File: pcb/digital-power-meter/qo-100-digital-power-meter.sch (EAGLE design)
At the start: 32 parts, among them U1 F2915NBGK, U2 ADP7142AUJZ-3.3

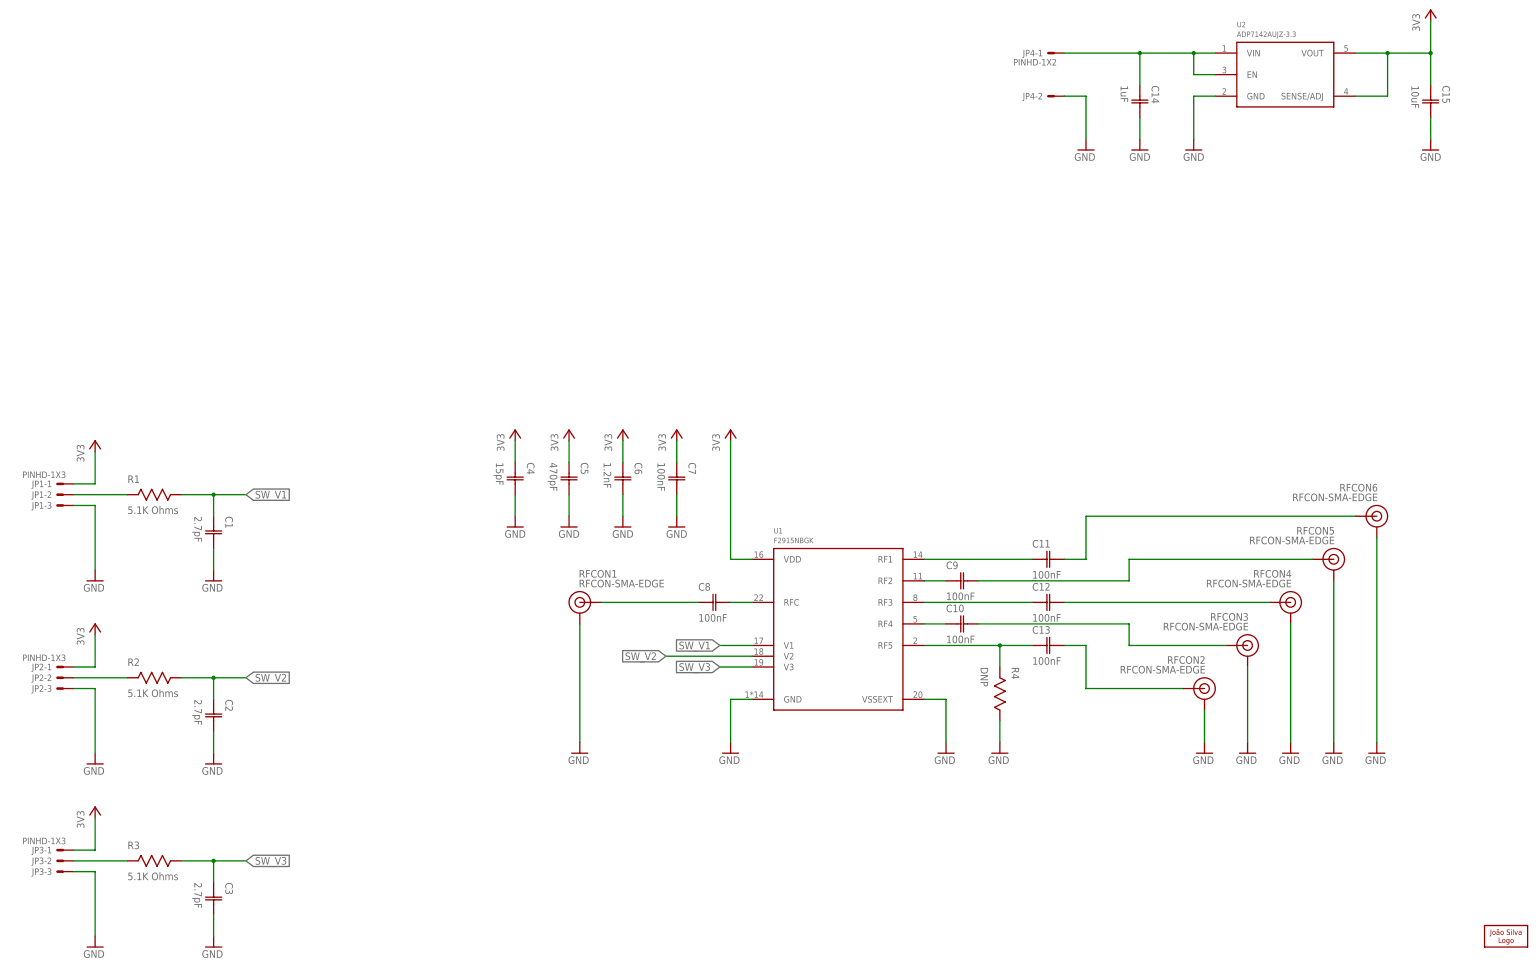
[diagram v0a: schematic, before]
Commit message: Finished RF switch Added Digital RF power detector Added Orange Pi control hat
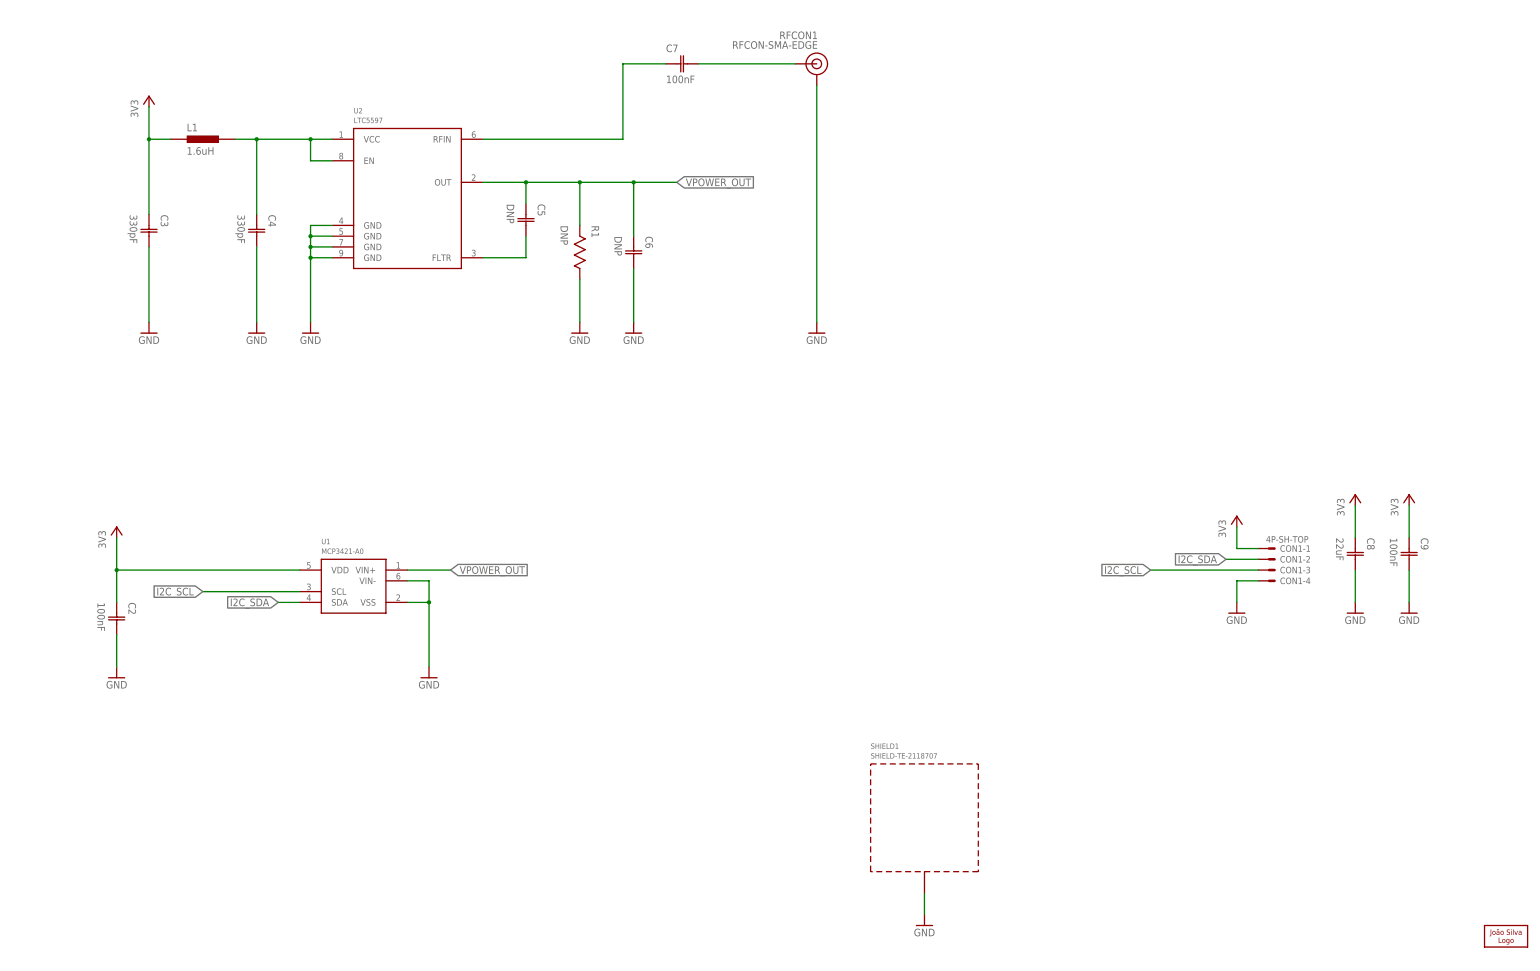
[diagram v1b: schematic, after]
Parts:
- removed C1: 2.7pF, Capacitor:CAPACITOR-0603
- removed C10, C11, C12, C13: 100nF, Capacitor:CAPACITOR-0603
- removed C14: 1uF, Capacitor:CAPACITOR-0603
- removed C15: 10uF, Capacitor:CAPACITOR-0603
- removed JP1, JP2, JP3: PINHD-1X3, Pin Header:PINHD-1X3
- removed JP4: PINHD-1X2, Pin Header:PINHD-1X2
- removed R2, R3: 5.1K Ohms, Resistor:RESISTOR-0603
- removed R4: DNP, Resistor:RESISTOR-0603
- removed RFCON2, RFCON3, RFCON4, RFCON5, RFCON6: RFCON-SMA-EDGE, RF Connector:RFCON-SMA-EDGE
- added CON1: 4P-SH-TOP, JST:4P-SH-TOP
- added L1: 1.6uH, Inductor:INDUCTOR-0603
- added SHIELD1: SHIELD-TE-2118707, Shield:SHIELD-TE-2118707
- C2: value 2.7pF -> 100nF
- C3: value 2.7pF -> 330pF
- C4: value 15pF -> 330pF
- C5: value 470pF -> DNP
- C6: value 1.2nF -> DNP
- C8: value 100nF -> 22uF; device Capacitor:CAPACITOR-0603 -> Capacitor:CAPACITOR-1206
- R1: value 5.1K Ohms -> DNP
- U1: value F2915NBGK -> MCP3421-A0; device Renesas:F2915NBGK -> Microchip:MCP3421-A0
- U2: value ADP7142AUJZ-3.3 -> LTC5597; device Analog Devices:ADP7142AUJZ-3.3 -> Analog Devices:LTC5597
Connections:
- removed net N$10: C12.C2, RFCON4.SIGNAL
- removed net N$11: C9.C2, RFCON5.SIGNAL
- removed net N$12: C11.C2, RFCON6.SIGNAL
- removed net N$13: JP1-2.S, R1.2
- removed net N$14: JP2-2.S, R2.2
- removed net N$15: JP3-2.S, R3.2
- removed net N$16: C14.C1, JP4-1.S, U2.EN, U2.VIN
- removed net N$5: C12.C1, U1.RF3
- removed net N$6: C9.C1, U1.RF2
- removed net N$7: C11.C1, U1.RF1
- removed net N$8: C13.C2, RFCON2.SIGNAL
- removed net N$9: C10.C2, RFCON3.SIGNAL
- removed net SW_V1: C1.C1, R1.1, U1.V1
- removed net SW_V2: C2.C1, R2.1, U1.V2
- removed net SW_V3: C3.C1, R3.1, U1.V3
- new net I2C_SCL: CON1-3.S, U1.SCL
- new net I2C_SDA: CON1-2.S, U1.SDA
- new net VPOWER_OUT: C5.C1, C6.C1, R1.2, U1.VIN+, U2.OUT
- net 3V3: now also C2.C1, C3.C1, C8.C1, C9.C1, CON1-1.S, L1.1; no longer C15.C1, C4.C1, C5.C1, C6.C1, C7.C1, JP1-1.S, JP2-1.S, JP3-1.S, U2.SENSE/ADJ, U2.VOUT
- net GND: now also C8.C2, C9.C2, CON1-4.S, R1.1, SHIELD1.GND, U1.VIN-, U1.VSS, U2.GND@0, U2.GND@1, U2.GND@2, U2.GND@3; no longer C1.C2, C14.C2, C15.C2, C5.C2, C7.C2, JP1-3.S, JP2-3.S, JP3-3.S, JP4-2.S, R4.1, RFCON2.GND, RFCON3.GND, RFCON4.GND, RFCON5.GND, RFCON6.GND, U1.GND, U1.VSSEXT, U2.GND
- net N$1: now also C7.C1, U2.RFIN; no longer C8.C1, RFCON1.SIGNAL
- net N$2: now also C7.C2, RFCON1.SIGNAL; no longer C8.C2, U1.RFC
- net N$3: now also C5.C2, U2.FLTR; no longer C13.C1, R4.2, U1.RF5
- net N$4: now also C4.C1, L1.2, U2.EN, U2.VCC; no longer C10.C1, U1.RF4
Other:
- note removed: "Install R4 for F2914 Do not install R4 for F2915"
- moved on the sheet: C2, C3, C4, C5, C6, C7, C8, C9, R1, RFCON1

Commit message: Renamed RF Power meter Added Power meter Added IO expander to RF switch PCB to make it work thru I2C
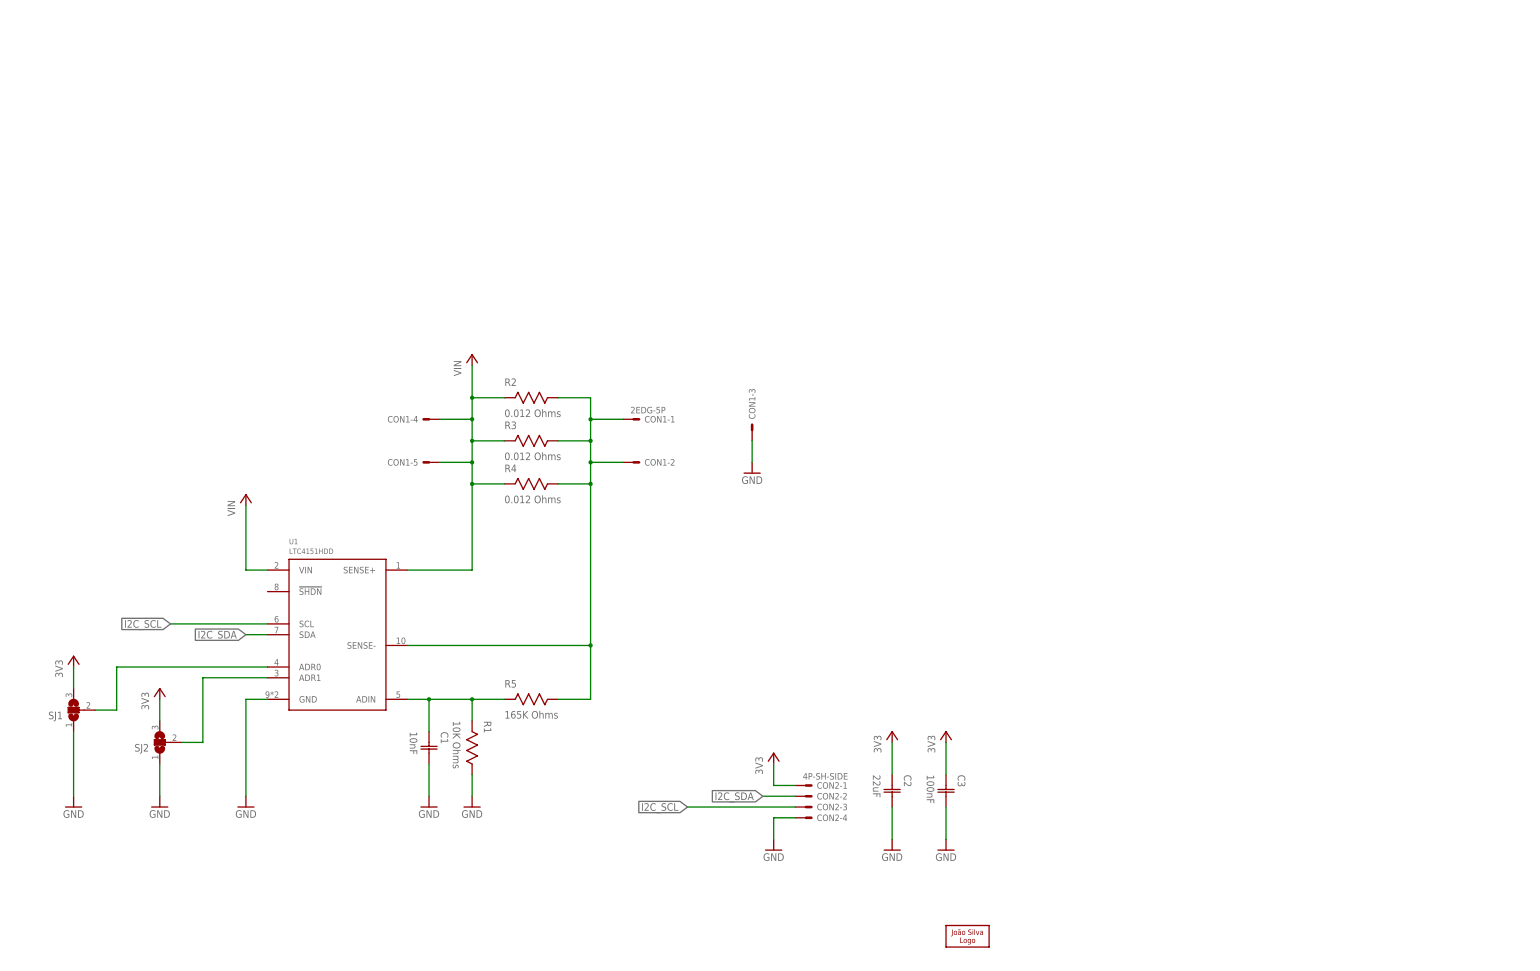
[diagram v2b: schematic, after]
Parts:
- removed C4: 330pF, Capacitor:CAPACITOR-0603
- removed C5, C6: DNP, Capacitor:CAPACITOR-0603
- removed C7, C9: 100nF, Capacitor:CAPACITOR-0603
- removed C8: 22uF, Capacitor:CAPACITOR-1206
- removed L1: 1.6uH, Inductor:INDUCTOR-0603
- removed RFCON1: RFCON-SMA-EDGE, RF Connector:RFCON-SMA-EDGE
- removed SHIELD1: SHIELD-TE-2118707, Shield:SHIELD-TE-2118707
- removed U2: LTC5597, Analog Devices:LTC5597
- added C1: 10nF, Capacitor:CAPACITOR-0603
- added CON2: 4P-SH-SIDE, JST:4P-SH-SIDE
- added R2, R3, R4: 0.012 Ohms, Resistor:RESISTOR-2512
- added R5: 165K Ohms, Resistor:RESISTOR-0603
- added SJ1, SJ2: (no value), Solder Jumper:SJ2S
- C2: value 100nF -> 22uF; device Capacitor:CAPACITOR-0603 -> Capacitor:CAPACITOR-1206
- C3: value 330pF -> 100nF
- CON1: value 4P-SH-TOP -> 2EDG-5P; device JST:4P-SH-TOP -> Generic Connector:2EDG-5P
- R1: value DNP -> 10K Ohms
- U1: value MCP3421-A0 -> LTC4151HDD; device Microchip:MCP3421-A0 -> Analog Devices:LTC4151HDD
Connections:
- removed net VPOWER_OUT: C5.C1, C6.C1, R1.2, U1.VIN+, U2.OUT
- new net VIN: CON1-4.S, CON1-5.S, R2.2, R3.2, R4.2, U1.SENSE+, U1.VIN
- net 3V3: now also CON2-1.S, SJ1.3, SJ2.3; no longer C8.C1, C9.C1, CON1-1.S, L1.1, U1.VDD
- net GND: now also C1.C2, CON1-3.S, CON2-4.S, SJ1.1, SJ2.1, U1.GND; no longer C4.C2, C6.C2, C8.C2, C9.C2, CON1-4.S, RFCON1.GND, SHIELD1.GND, U1.VIN-, U1.VSS, U2.GND@0, U2.GND@1, U2.GND@2, U2.GND@3
- net I2C_SCL: now also CON2-3.S; no longer CON1-3.S
- net I2C_SDA: now also CON2-2.S; no longer CON1-2.S
- net N$1: now also C1.C1, R1.2, R5.2, U1.ADIN; no longer C7.C1, U2.RFIN
- net N$2: now also CON1-1.S, CON1-2.S, R2.1, R3.1, R4.1, R5.1, U1.SENSE-; no longer C7.C2, RFCON1.SIGNAL
- net N$3: now also SJ1.2, U1.ADR0; no longer C5.C2, U2.FLTR
- net N$4: now also SJ2.2, U1.ADR1; no longer C4.C1, L1.2, U2.EN, U2.VCC
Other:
- moved on the sheet: C2, C3, CON1-1, CON1-2, CON1-3, CON1-4, R1

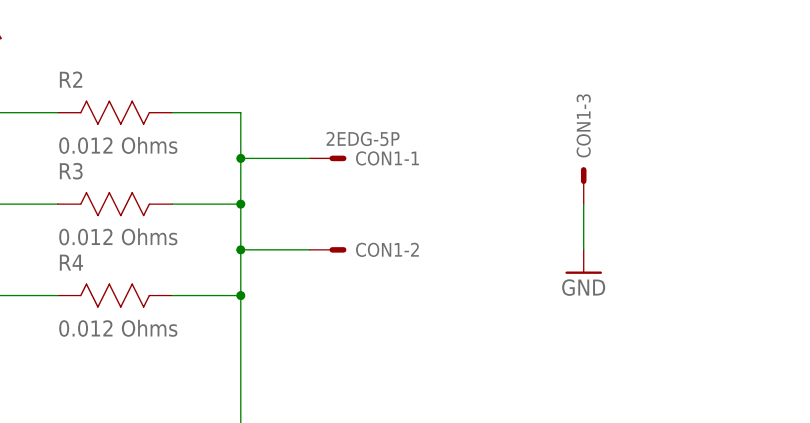
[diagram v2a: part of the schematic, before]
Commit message: Update 2EDG connector on power meter
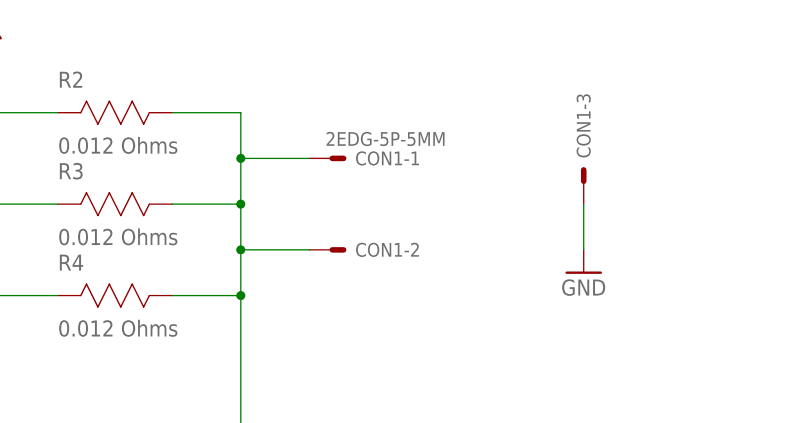
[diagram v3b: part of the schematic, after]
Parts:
- CON1: value 2EDG-5P -> 2EDG-5P-5MM; device Generic Connector:2EDG-5P -> Generic Connector:2EDG-5P-5MM
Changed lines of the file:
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@@
 <part name="R3" library="Resistor" deviceset="RESISTOR" device="-2512" value="0.012 Ohms"/>
 <part name="R4" library="Resistor" deviceset="RESISTOR" device="-2512" value="0.012 Ohms"/>
-<part name="CON1" library="Generic Connector" deviceset="2EDG-5P" device=""/>
+<part name="CON1" library="Generic Connector" deviceset="2EDG-5P" device="-5MM"/>
 <part name="U1" library="Analog Devices" deviceset="LTC4151*?" device="DD" technology="H"/>
 <part name="GND2" library="Supply Symbol" deviceset="GND" device=""/>
